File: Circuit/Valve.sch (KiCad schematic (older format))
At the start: 20 parts, among them CN1 GROVE, CN2 ST-LINK, CN3 TTL-232R-3V3, SW1 RESET, U1 STM32L010F4P6

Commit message: フットプリントの関連付け
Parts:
- C1: renamed from C?; footprint (none) -> Capacitor_THT:C_Disc_D5.0mm_W2.5mm_P2.50mm
- C2: renamed from C?; footprint (none) -> Capacitor_THT:CP_Radial_D5.0mm_P2.50mm
- CN1: footprint (none) -> OPL_Connector:HW4-2.0-90D
- CN2, CN3: footprint (none) -> Connector_PinHeader_2.54mm:PinHeader_1x06_P2.54mm_Vertical
- H1, H2, H3, H4: footprint (none) -> MountingHole:MountingHole_3.2mm_M3
- J1: renamed from J?; footprint (none) -> Connector_PinHeader_2.54mm:PinHeader_1x02_P2.54mm_Vertical
- JP1, JP2: footprint (none) -> Jumper:SolderJumper-2_P1.3mm_Open_TrianglePad1.0x1.5mm
- RE1, RE2, RE3, RE4: footprint (none) -> extsui:EC12PLRGB
- SW1: footprint (none) -> Button_Switch_THT:SW_PUSH_6mm_H8mm
- TP1, TP2: footprint (none) -> Connector_PinHeader_2.54mm:PinHeader_1x10_P2.54mm_Vertical
- U1: footprint (none) -> Package_SO:TSSOP-20_4.4x6.5mm_P0.65mm
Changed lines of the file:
@@
 F 0 "RE1" H 2672 4697 60  0000 R CNN
 F 1 "EC12PLRGB" H 2672 4803 60  0000 R CNN
-F 2 "" H 3100 4850 60  0000 C CNN
+F 2 "extsui:EC12PLRGB" H 3100 4850 60  0001 C CNN
 F 3 "" H 3100 4850 60  0000 C CNN
 	1    3100 4750
@@
 F 0 "RE2" H 4172 4697 60  0000 R CNN
 F 1 "EC12PLRGB" H 4172 4803 60  0000 R CNN
-F 2 "" H 4600 4850 60  0000 C CNN
+F 2 "extsui:EC12PLRGB" H 4600 4850 60  0001 C CNN
 F 3 "" H 4600 4850 60  0000 C CNN
 	1    4600 4750
@@
 F 0 "RE3" H 5672 4697 60  0000 R CNN
 F 1 "EC12PLRGB" H 5672 4803 60  0000 R CNN
-F 2 "" H 6100 4850 60  0000 C CNN
+F 2 "extsui:EC12PLRGB" H 6100 4850 60  0001 C CNN
 F 3 "" H 6100 4850 60  0000 C CNN
 	1    6100 4750
@@
 F 0 "RE4" H 7172 4697 60  0000 R CNN
 F 1 "EC12PLRGB" H 7172 4803 60  0000 R CNN
-F 2 "" H 7600 4850 60  0000 C CNN
+F 2 "extsui:EC12PLRGB" H 7600 4850 60  0001 C CNN
 F 3 "" H 7600 4850 60  0000 C CNN
 	1    7600 4750
@@
 F 0 "CN3" H 10173 3623 50  0000 R CNN
 F 1 "TTL-232R-3V3" H 10173 3532 50  0000 R CNN
-F 2 "" H 10200 3650 50  0001 C CNN
+F 2 "Connector_PinHeader_2.54mm:PinHeader_1x06_P2.54mm_Vertical" H 10200 3650 50  0001 C CNN
 F 3 "~" H 10200 3650 50  0001 C CNN
 	1    10200 3650
@@
 F 0 "CN2" H 1723 5073 50  0000 R CNN
 F 1 "ST-LINK" H 1723 4982 50  0000 R CNN
-F 2 "" H 1750 5100 50  0001 C CNN
+F 2 "Connector_PinHeader_2.54mm:PinHeader_1x06_P2.54mm_Vertical" H 1750 5100 50  0001 C CNN
 F 3 "~" H 1750 5100 50  0001 C CNN
 	1    1750 5100
@@
 F 0 "CN1" H 920 4117 50  0000 C CNN
 F 1 "GROVE" H 920 4026 50  0000 C CNN
-F 2 "" H 1000 3800 50  0001 C CNN
+F 2 "OPL_Connector:HW4-2.0-90D" H 1000 3800 50  0001 C CNN
 F 3 "~" H 1000 3800 50  0001 C CNN
 	1    1000 3800
@@
 F 0 "U1" H 5800 3015 50  0000 C CNN
 F 1 "STM32L010F4P6" H 5800 2924 50  0000 C CNN
-F 2 "" H 5750 2550 50  0001 C CNN
+F 2 "Package_SO:TSSOP-20_4.4x6.5mm_P0.65mm" H 5750 2550 50  0001 C CNN
 F 3 "" H 5750 2550 50  0001 C CNN
 	1    5800 2250
@@
 F 0 "TP1" V 4335 1076 50  0000 C CNN
 F 1 "Conn_01x10_Male_DebugPad" V 4426 1076 50  0000 C CNN
-F 2 "" H 4500 1150 50  0001 C CNN
+F 2 "Connector_PinHeader_2.54mm:PinHeader_1x10_P2.54mm_Vertical" H 4500 1150 50  0001 C CNN
 F 3 "~" H 4500 1150 50  0001 C CNN
 	1    4500 1150
@@
 F 0 "TP2" V 6935 1077 50  0000 C CNN
 F 1 "Conn_01x10_Male_DebugPad" V 7026 1077 50  0000 C CNN
-F 2 "" H 7100 1150 50  0001 C CNN
+F 2 "Connector_PinHeader_2.54mm:PinHeader_1x10_P2.54mm_Vertical" H 7100 1150 50  0001 C CNN
 F 3 "~" H 7100 1150 50  0001 C CNN
 	1    7100 1150
@@
 F 0 "JP1" H 10200 1535 50  0000 C CNN
 F 1 "I2C_ADDR_A0" H 10200 1444 50  0000 C CNN
-F 2 "" H 10200 1350 50  0001 C CNN
+F 2 "Jumper:SolderJumper-2_P1.3mm_Open_TrianglePad1.0x1.5mm" H 10200 1350 50  0001 C CNN
 F 3 "~" H 10200 1350 50  0001 C CNN
 	1    10200 1350
@@
 F 0 "JP2" H 10200 1835 50  0000 C CNN
 F 1 "I2C_ADDR_A1" H 10200 1744 50  0000 C CNN
-F 2 "" H 10200 1650 50  0001 C CNN
+F 2 "Jumper:SolderJumper-2_P1.3mm_Open_TrianglePad1.0x1.5mm" H 10200 1650 50  0001 C CNN
 F 3 "~" H 10200 1650 50  0001 C CNN
 	1    10200 1650
@@
 F 0 "H1" H 1200 6196 50  0000 L CNN
 F 1 "MountingHole" H 1200 6105 50  0000 L CNN
-F 2 "" H 1100 6150 50  0001 C CNN
+F 2 "MountingHole:MountingHole_3.2mm_M3" H 1100 6150 50  0001 C CNN
 F 3 "~" H 1100 6150 50  0001 C CNN
 	1    1100 6150
@@
 F 0 "H2" H 1200 6496 50  0000 L CNN
 F 1 "MountingHole" H 1200 6405 50  0000 L CNN
-F 2 "" H 1100 6450 50  0001 C CNN
+F 2 "MountingHole:MountingHole_3.2mm_M3" H 1100 6450 50  0001 C CNN
 F 3 "~" H 1100 6450 50  0001 C CNN
 	1    1100 6450
@@
 F 0 "H3" H 1200 6796 50  0000 L CNN
 F 1 "MountingHole" H 1200 6705 50  0000 L CNN
-F 2 "" H 1100 6750 50  0001 C CNN
+F 2 "MountingHole:MountingHole_3.2mm_M3" H 1100 6750 50  0001 C CNN
 F 3 "~" H 1100 6750 50  0001 C CNN
 	1    1100 6750
@@
 F 0 "H4" H 1200 7096 50  0000 L CNN
 F 1 "MountingHole" H 1200 7005 50  0000 L CNN
-F 2 "" H 1100 7050 50  0001 C CNN
+F 2 "MountingHole:MountingHole_3.2mm_M3" H 1100 7050 50  0001 C CNN
 F 3 "~" H 1100 7050 50  0001 C CNN
 	1    1100 7050
@@
 F 0 "SW1" H 3400 2035 50  0000 C CNN
 F 1 "RESET" H 3400 1944 50  0000 C CNN
-F 2 "" H 3400 1950 50  0001 C CNN
+F 2 "Button_Switch_THT:SW_PUSH_6mm_H8mm" H 3400 1950 50  0001 C CNN
 F 3 "" H 3400 1950 50  0001 C CNN
 	1    3400 1750
@@
 	10200 1000 10200 1100
 $Comp
-L Connector:Conn_01x02_Male J?
+L Connector:Conn_01x02_Male J1
 U 1 1 61C6BFB2
 P 950 2200
-F 0 "J?" H 1200 2500 50  0000 C CNN
+F 0 "J1" H 1200 2500 50  0000 C CNN
 F 1 "Conn_01x02_Male" H 1200 2400 50  0000 C CNN
-F 2 "" H 950 2200 50  0001 C CNN
+F 2 "Connector_PinHeader_2.54mm:PinHeader_1x02_P2.54mm_Vertical" H 950 2200 50  0001 C CNN
 F 3 "~" H 950 2200 50  0001 C CNN
 	1    950  2200
@@
 $EndComp
 $Comp
-L Device:C_Small C?
+L Device:C_Small C1
 U 1 1 61C6C2A7
 P 1500 2400
-F 0 "C?" H 1592 2446 50  0000 L CNN
+F 0 "C1" H 1592 2446 50  0000 L CNN
 F 1 "0.1u" H 1592 2355 50  0000 L CNN
-F 2 "" H 1500 2400 50  0001 C CNN
+F 2 "Capacitor_THT:C_Disc_D5.0mm_W2.5mm_P2.50mm" H 1500 2400 50  0001 C CNN
 F 3 "~" H 1500 2400 50  0001 C CNN
 	1    1500 2400
@@
 $EndComp
 $Comp
-L Device:CP_Small C?
+L Device:CP_Small C2
 U 1 1 61C6D6C3
 P 1900 2400
-F 0 "C?" H 1988 2446 50  0000 L CNN
+F 0 "C2" H 1988 2446 50  0000 L CNN
 F 1 "47u" H 1988 2355 50  0000 L CNN
-F 2 "" H 1900 2400 50  0001 C CNN
+F 2 "Capacitor_THT:CP_Radial_D5.0mm_P2.50mm" H 1900 2400 50  0001 C CNN
 F 3 "~" H 1900 2400 50  0001 C CNN
 	1    1900 2400
@@
 	800  3000 800  1700
 $Comp
-L power:GND #PWR?
+L power:GND #PWR0107
 U 1 1 61C98924
 P 1500 2700
-F 0 "#PWR?" H 1500 2450 50  0001 C CNN
+F 0 "#PWR0107" H 1500 2450 50  0001 C CNN
 F 1 "GND" H 1505 2527 50  0000 C CNN
 F 2 "" H 1500 2700 50  0001 C CNN

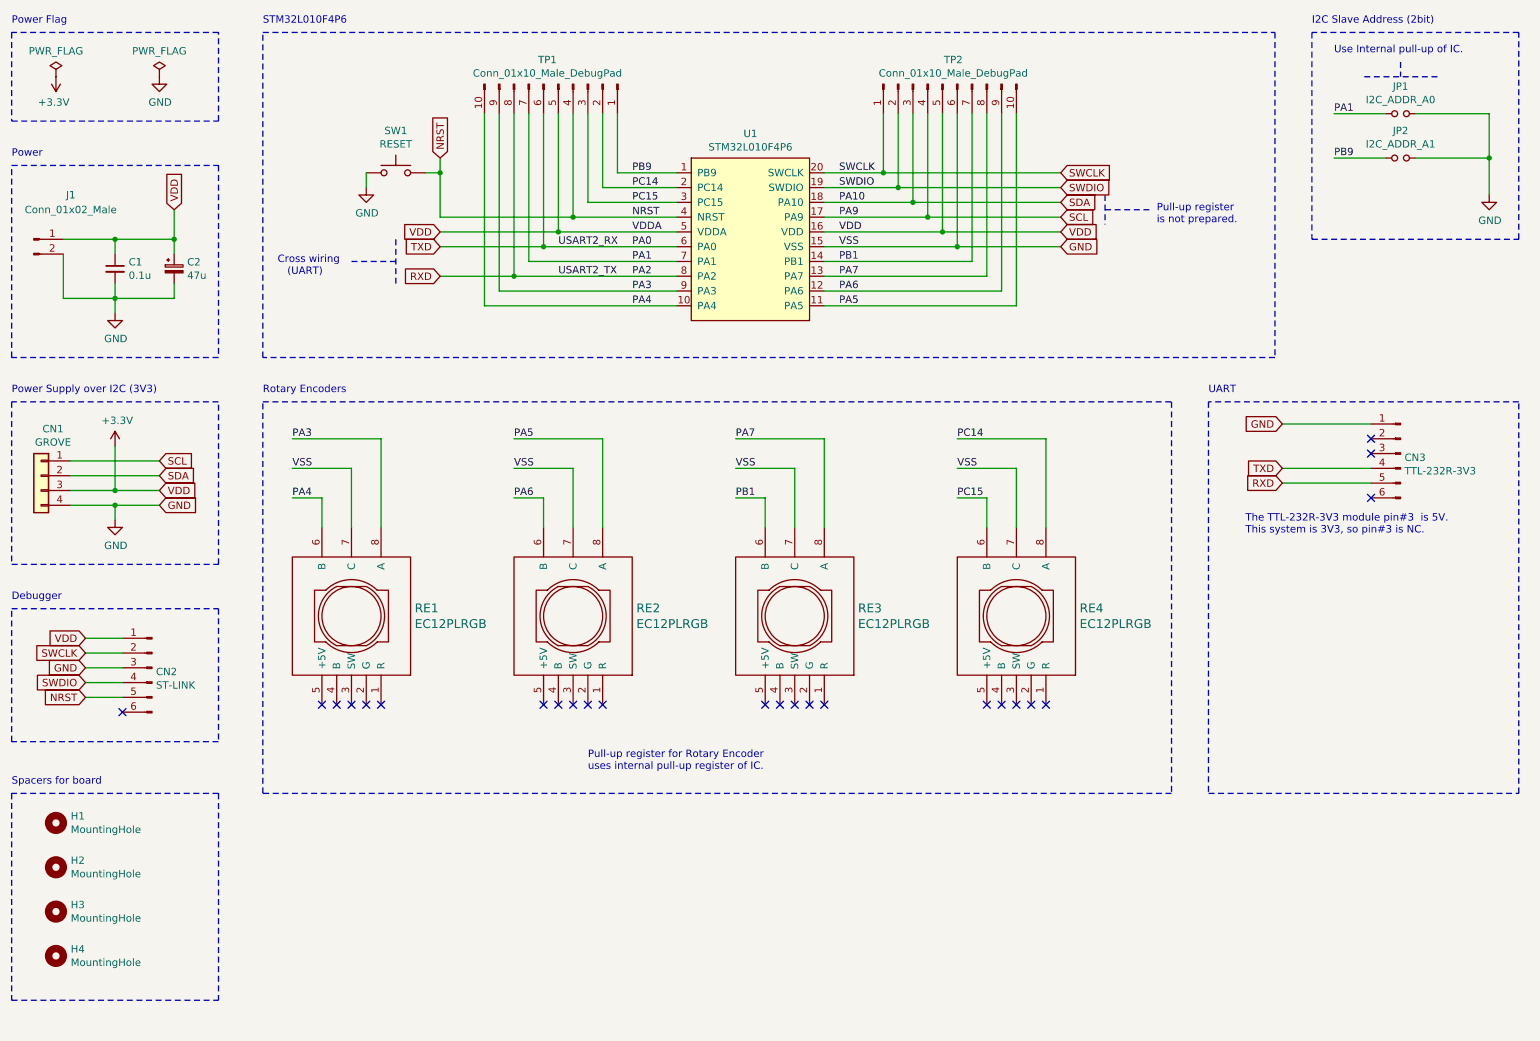
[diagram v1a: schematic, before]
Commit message: 回路図を修正
* 電源コネクタ (2P) を I2C 兼用 4P に変更
* I2C ADDR パッドを削除して LED と抵抗に置換
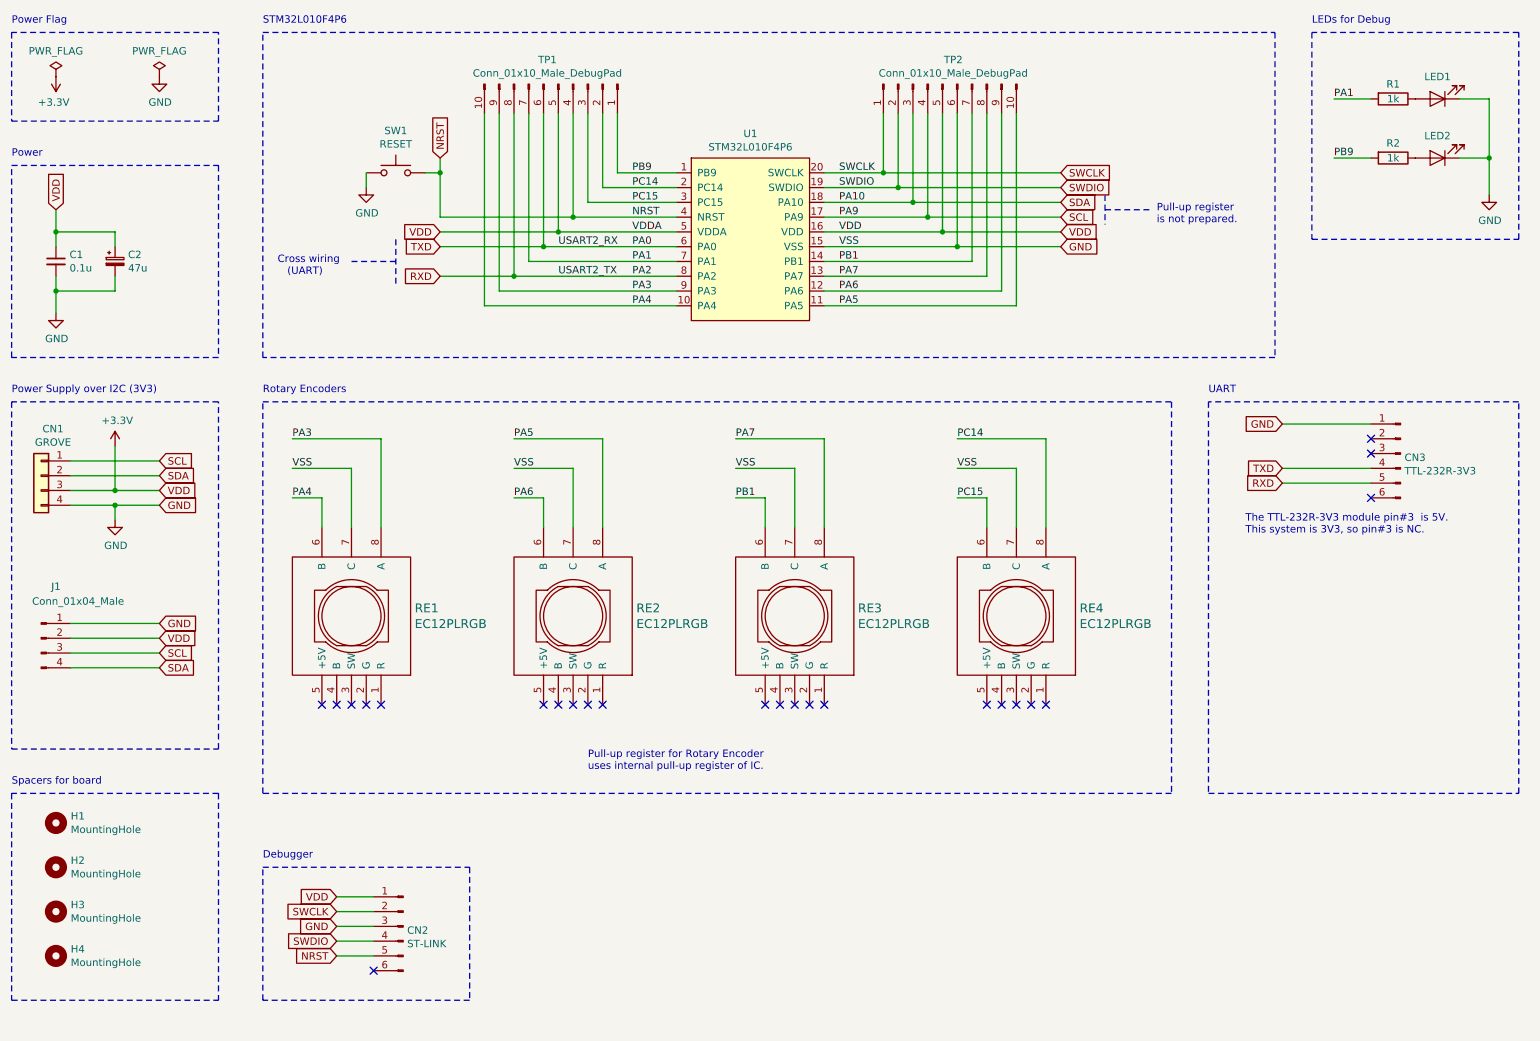
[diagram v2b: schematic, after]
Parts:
- removed J1: Conn_01x02_Male, Connector_PinHeader_2.54mm:PinHeader_1x02_P2.54mm_Vertical, symbol Connector:Conn_01x02_Male
- removed JP1: I2C_ADDR_A0, Jumper:SolderJumper-2_P1.3mm_Open_TrianglePad1.0x1.5mm, symbol Device:Jumper_NO_Small
- removed JP2: I2C_ADDR_A1, Jumper:SolderJumper-2_P1.3mm_Open_TrianglePad1.0x1.5mm, symbol Device:Jumper_NO_Small
- added J1: Conn_01x04_Male, Connector_PinHeader_2.54mm:PinHeader_1x04_P2.54mm_Vertical, symbol Connector:Conn_01x04_Male
- added LED1, LED2: LED, LED_THT:LED_D3.0mm, symbol Device:LED
- added R1, R2: 1k, Resistor_THT:R_Axial_DIN0207_L6.3mm_D2.5mm_P7.62mm_Horizontal, symbol Device:R
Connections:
- net +3V3: now also J1.2 (Pin_2)
- net GND: now also J1.1 (Pin_1), LED1.1 (K), LED2.1 (K)
- net PA1: now also R1.2
- net PB9: now also R2.2
- net SCL: now also J1.3 (Pin_3)
- net SDA: now also J1.4 (Pin_4)
- new net: LED1.2 (A), R1.1
- new net: LED2.2 (A), R2.1
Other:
- note added: "LEDs for Debug"
- note removed: "I2C Slave Address (2bit)"
- note removed: "Use Internal pull-up of IC."
- moved on the sheet: C1, C2, CN2
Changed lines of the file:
@@
 L Connector:Conn_01x06_Male CN2
 U 1 1 61C0B8EC
-P 1750 5100
-F 0 "CN2" H 1723 5073 50  0000 R CNN
-F 1 "ST-LINK" H 1723 4982 50  0000 R CNN
-F 2 "Connector_PinHeader_2.54mm:PinHeader_1x06_P2.54mm_Vertical" H 1750 5100 50  0001 C CNN
-F 3 "~" H 1750 5100 50  0001 C CNN
-	1    1750 5100
+P 3450 6850
+F 0 "CN2" H 3423 6823 50  0000 R CNN
+F 1 "ST-LINK" H 3423 6732 50  0000 R CNN
+F 2 "Connector_PinHeader_2.54mm:PinHeader_1x06_P2.54mm_Vertical" H 3450 6850 50  0001 C CNN
+F 3 "~" H 3450 6850 50  0001 C CNN
+	1    3450 6850
 	-1   0    0    -1
 $EndComp
@@
 NoConn ~ 7700 5350
 NoConn ~ 7800 5350
-Text GLabel 1300 4900 0    50   Input ~ 0
+Text GLabel 3000 6650 0    50   Input ~ 0
 VDD
-Text GLabel 1300 5000 0    50   Input ~ 0
+Text GLabel 3000 6750 0    50   Input ~ 0
 SWCLK
-Text GLabel 1300 5100 0    50   Input ~ 0
+Text GLabel 3000 6850 0    50   Input ~ 0
 GND
-Text GLabel 1300 5200 0    50   Input ~ 0
+Text GLabel 3000 6950 0    50   Input ~ 0
 SWDIO
-Text GLabel 1300 5300 0    50   Input ~ 0
+Text GLabel 3000 7050 0    50   Input ~ 0
 NRST
-NoConn ~ 1550 5400
+NoConn ~ 3250 7150
 Wire Wire Line
-	1300 4900 1550 4900
+	3000 6650 3250 6650
 Wire Wire Line
-	1550 5000 1300 5000
+	3250 6750 3000 6750
 Wire Wire Line
-	1300 5100 1550 5100
+	3000 6850 3250 6850
 Wire Wire Line
-	1550 5200 1300 5200
+	3250 6950 3000 6950
 Wire Wire Line
-	1300 5300 1550 5300
+	3000 7050 3250 7050
 $Comp
 L extsui:STM32L010F4P6 U1
@@
 Text Notes 9150 4200 0    50   ~ 0
 The TTL-232R-3V3 module pin#3  is 5V.\nThis system is 3V3, so pin#3 is NC.
-$Comp
-L Device:Jumper_NO_Small JP1
-U 1 1 61C572FE
-P 10200 1350
-F 0 "JP1" H 10200 1535 50  0000 C CNN
-F 1 "I2C_ADDR_A0" H 10200 1444 50  0000 C CNN
-F 2 "Jumper:SolderJumper-2_P1.3mm_Open_TrianglePad1.0x1.5mm" H 10200 1350 50  0001 C CNN
-F 3 "~" H 10200 1350 50  0001 C CNN
-	1    10200 1350
-	1    0    0    -1
-$EndComp
-$Comp
-L Device:Jumper_NO_Small JP2
-U 1 1 61C57349
-P 10200 1650
-F 0 "JP2" H 10200 1835 50  0000 C CNN
-F 1 "I2C_ADDR_A1" H 10200 1744 50  0000 C CNN
-F 2 "Jumper:SolderJumper-2_P1.3mm_Open_TrianglePad1.0x1.5mm" H 10200 1650 50  0001 C CNN
-F 3 "~" H 10200 1650 50  0001 C CNN
-	1    10200 1650
-	1    0    0    -1
-$EndComp
 Wire Wire Line
 	7400 3950 7400 4150
@@
 Power Supply over I2C (3V3)
 Wire Notes Line
-	800  3300 800  4400
+	800  3300 800  5650
 Wire Notes Line
-	800  4400 2200 4400
+	800  5650 2200 5650
 Wire Notes Line
-	2200 4400 2200 3300
+	2200 5650 2200 3300
 Wire Notes Line
 	2200 3300 800  3300
@@
 	3700 1750 3700 1650
 Wire Notes Line
-	2200 5600 800  5600
+	3900 7350 2500 7350
 Wire Notes Line
-	800  5600 800  4700
+	2500 7350 2500 6450
 Wire Notes Line
-	800  4700 2200 4700
+	2500 6450 3900 6450
 Wire Notes Line
-	2200 4700 2200 5600
+	3900 6450 3900 7350
 Wire Notes Line
 	11000 5950 11000 3300
@@
 	8900 5950 11000 5950
 Wire Wire Line
-	10300 1350 10800 1350
+	10600 1250 10800 1250
 Wire Wire Line
-	10800 1350 10800 1650
+	10800 1250 10800 1650
 Wire Wire Line
-	10300 1650 10800 1650
+	10600 1650 10800 1650
 Connection ~ 10800 1650
 Wire Wire Line
@@
 $EndComp
 Wire Wire Line
-	10100 1350 9750 1350
+	10000 1250 9750 1250
 Wire Wire Line
-	10100 1650 9750 1650
-Text Label 9750 1350 0    50   ~ 0
+	10000 1650 9750 1650
+Text Label 9750 1250 0    50   ~ 0
 PA1
 Text Label 9750 1650 0    50   ~ 0
@@
 Text Label 4500 2250 0    50   ~ 0
 USART2_RX
-Text Notes 800  4650 0    50   ~ 0
+Text Notes 2500 6400 0    50   ~ 0
 Debugger
 Wire Notes Line
@@
 Wire Notes Line
 	11000 800  9600 800
-Text Notes 9750 950  0    50   ~ 0
-Use Internal pull-up of IC.
 Text Notes 9600 750  0    50   ~ 0
-I2C Slave Address (2bit)
-Wire Notes Line
-	10450 1100 9950 1100
-Wire Notes Line
-	10200 1000 10200 1100
-$Comp
-L Connector:Conn_01x02_Male J1
-U 1 1 61C6BFB2
-P 950 2200
-F 0 "J1" H 1200 2500 50  0000 C CNN
-F 1 "Conn_01x02_Male" H 1200 2400 50  0000 C CNN
-F 2 "Connector_PinHeader_2.54mm:PinHeader_1x02_P2.54mm_Vertical" H 950 2200 50  0001 C CNN
-F 3 "~" H 950 2200 50  0001 C CNN
-	1    950  2200
-	1    0    0    -1
-$EndComp
+LEDs for Debug
 $Comp
 L Device:C_Small C1
 U 1 1 61C6C2A7
-P 1500 2400
-F 0 "C1" H 1592 2446 50  0000 L CNN
-F 1 "0.1u" H 1592 2355 50  0000 L CNN
-F 2 "Capacitor_THT:C_Disc_D5.0mm_W2.5mm_P2.50mm" H 1500 2400 50  0001 C CNN
-F 3 "~" H 1500 2400 50  0001 C CNN
-	1    1500 2400
+P 1100 2350
+F 0 "C1" H 1192 2396 50  0000 L CNN
+F 1 "0.1u" H 1192 2305 50  0000 L CNN
+F 2 "Capacitor_THT:C_Disc_D5.0mm_W2.5mm_P2.50mm" H 1100 2350 50  0001 C CNN
+F 3 "~" H 1100 2350 50  0001 C CNN
+	1    1100 2350
 	1    0    0    -1
 $EndComp
@@
 L Device:CP_Small C2
 U 1 1 61C6D6C3
-P 1900 2400
-F 0 "C2" H 1988 2446 50  0000 L CNN
-F 1 "47u" H 1988 2355 50  0000 L CNN
-F 2 "Capacitor_THT:CP_Radial_D5.0mm_P2.50mm" H 1900 2400 50  0001 C CNN
-F 3 "~" H 1900 2400 50  0001 C CNN
-	1    1900 2400
+P 1500 2350
+F 0 "C2" H 1588 2396 50  0000 L CNN
+F 1 "47u" H 1588 2305 50  0000 L CNN
+F 2 "Capacitor_THT:CP_Radial_D5.0mm_P2.50mm" H 1500 2350 50  0001 C CNN
+F 3 "~" H 1500 2350 50  0001 C CNN
+	1    1500 2350
 	1    0    0    -1
 $EndComp
@@
 L power:GND #PWR0107
 U 1 1 61C98924
-P 1500 2700
-F 0 "#PWR0107" H 1500 2450 50  0001 C CNN
-F 1 "GND" H 1505 2527 50  0000 C CNN
-F 2 "" H 1500 2700 50  0001 C CNN
-F 3 "" H 1500 2700 50  0001 C CNN
-	1    1500 2700
+P 1100 2700
+F 0 "#PWR0107" H 1100 2450 50  0001 C CNN
+F 1 "GND" H 1105 2527 50  0000 C CNN
+F 2 "" H 1100 2700 50  0001 C CNN
+F 3 "" H 1100 2700 50  0001 C CNN
+	1    1100 2700
 	1    0    0    -1
 $EndComp
 Wire Wire Line
-	1500 2500 1500 2600
+	1100 2450 1100 2550
 Wire Wire Line
-	1900 2600 1500 2600
+	1500 2550 1100 2550
 Wire Wire Line
-	1500 2600 1500 2700
-Connection ~ 1500 2600
+	1100 2550 1100 2700
+Connection ~ 1100 2550
 Wire Wire Line
-	1900 2200 1900 2300
-Connection ~ 1900 2200
+	1500 2150 1500 2250
 Wire Wire Line
-	1900 2200 1500 2200
+	1500 2150 1100 2150
 Wire Wire Line
-	1150 2600 1500 2600
-Wire Wire Line
-	1900 2600 1900 2500
+	1500 2550 1500 2450
 Text Notes 800  1650 0    50   ~ 0
 Power
-Text GLabel 1900 2000 1    50   Input ~ 0
+Text GLabel 1100 2000 1    50   Input ~ 0
 VDD
 Wire Wire Line
-	1900 2000 1900 2200
+	1100 2000 1100 2150
 Wire Wire Line
-	1150 2300 1150 2600
+	1100 2150 1100 2250
+$Comp
+L Device:R R1
+U 1 1 61D4C863
+P 10150 1250
+F 0 "R1" V 10050 1250 50  0000 C CNN
+F 1 "1k" V 10150 1250 50  0000 C CNN
+F 2 "Resistor_THT:R_Axial_DIN0207_L6.3mm_D2.5mm_P7.62mm_Horizontal" V 10080 1250 50  0001 C CNN
+F 3 "~" H 10150 1250 50  0001 C CNN
+	1    10150 1250
+	0    1    1    0
+$EndComp
+$Comp
+L Device:LED LED1
+U 1 1 61D4CAA3
+P 10450 1250
+F 0 "LED1" H 10450 1100 50  0000 C CNN
+F 1 "LED" H 10442 1086 50  0001 C CNN
+F 2 "LED_THT:LED_D3.0mm" H 10450 1250 50  0001 C CNN
+F 3 "~" H 10450 1250 50  0001 C CNN
+	1    10450 1250
+	-1   0    0    1
+$EndComp
+$Comp
+L Device:R R2
+U 1 1 61D5834E
+P 10150 1650
+F 0 "R2" V 10050 1650 50  0000 C CNN
+F 1 "1k" V 10150 1650 50  0000 C CNN
+F 2 "Resistor_THT:R_Axial_DIN0207_L6.3mm_D2.5mm_P7.62mm_Horizontal" V 10080 1650 50  0001 C CNN
+F 3 "~" H 10150 1650 50  0001 C CNN
+	1    10150 1650
+	0    1    1    0
+$EndComp
+$Comp
+L Device:LED LED2
+U 1 1 61D58355
+P 10450 1650
+F 0 "LED2" H 10450 1500 50  0000 C CNN
+F 1 "LED" H 10442 1486 50  0001 C CNN
+F 2 "LED_THT:LED_D3.0mm" H 10450 1650 50  0001 C CNN
+F 3 "~" H 10450 1650 50  0001 C CNN
+	1    10450 1650
+	-1   0    0    1
+$EndComp
+$Comp
+L Connector:Conn_01x04_Male J1
+U 1 1 61D809D8
+P 1000 4900
+F 0 "J1" H 1100 5250 50  0000 C CNN
+F 1 "Conn_01x04_Male" H 1250 5150 50  0000 C CNN
+F 2 "Connector_PinHeader_2.54mm:PinHeader_1x04_P2.54mm_Vertical" H 1000 4900 50  0001 C CNN
+F 3 "~" H 1000 4900 50  0001 C CNN
+	1    1000 4900
+	1    0    0    -1
+$EndComp
+Connection ~ 1100 2150
+Text GLabel 1800 5000 2    50   Input ~ 0
+SCL
+Text GLabel 1800 5100 2    50   Input ~ 0
+SDA
+Text GLabel 1800 4800 2    50   Input ~ 0
+GND
+Wire Wire Line
+	1800 4800 1200 4800
 Wire Wire Line
-	1500 2200 1500 2300
-Connection ~ 1500 2200
+	1200 4900 1800 4900
+Wire Wire Line
+	1800 5100 1200 5100
+Text GLabel 1800 4900 2    50   Input ~ 0
+VDD
 Wire Wire Line
-	1500 2200 1150 2200
+	1800 5000 1200 5000
 $EndSCHEMATC
